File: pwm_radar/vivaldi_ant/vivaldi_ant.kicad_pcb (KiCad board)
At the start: 2 copper layers, 49.6 x 39.1 mm, 0 parts

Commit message: vivaldi antenna put in
vivaldi antenna put in
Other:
- board outline removed

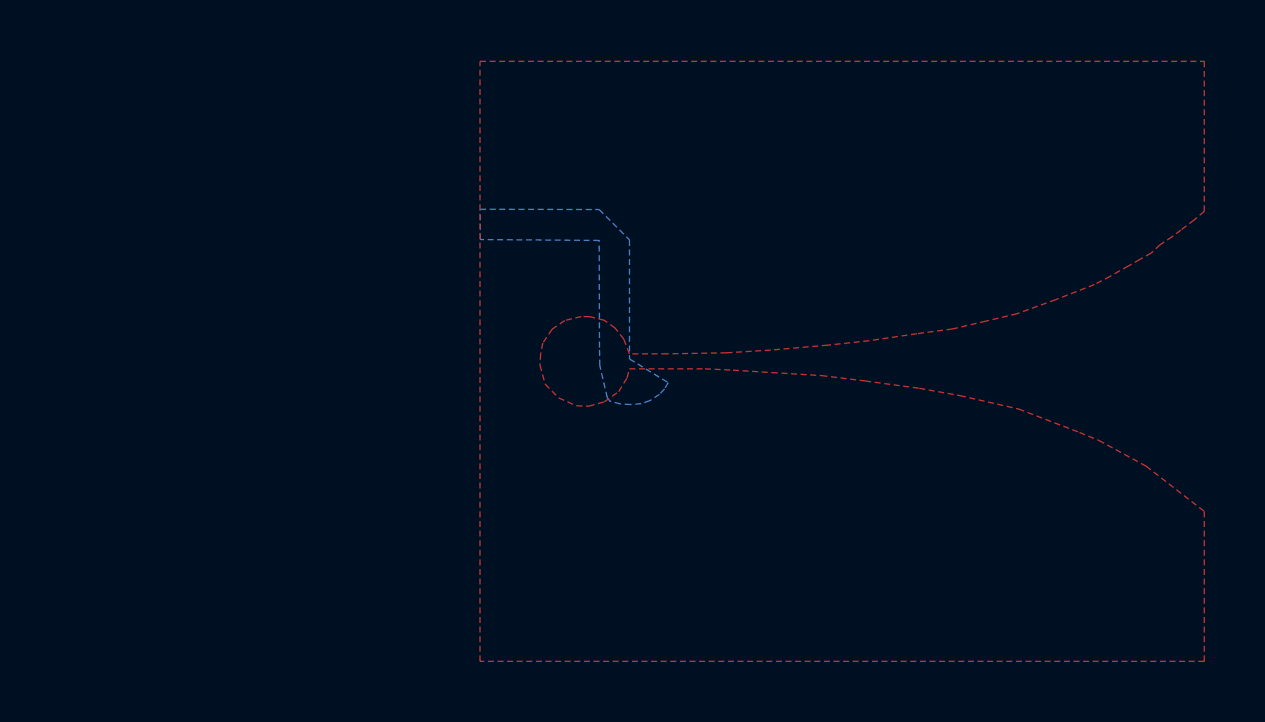
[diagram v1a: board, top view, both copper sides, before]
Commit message: added ant
added antenna
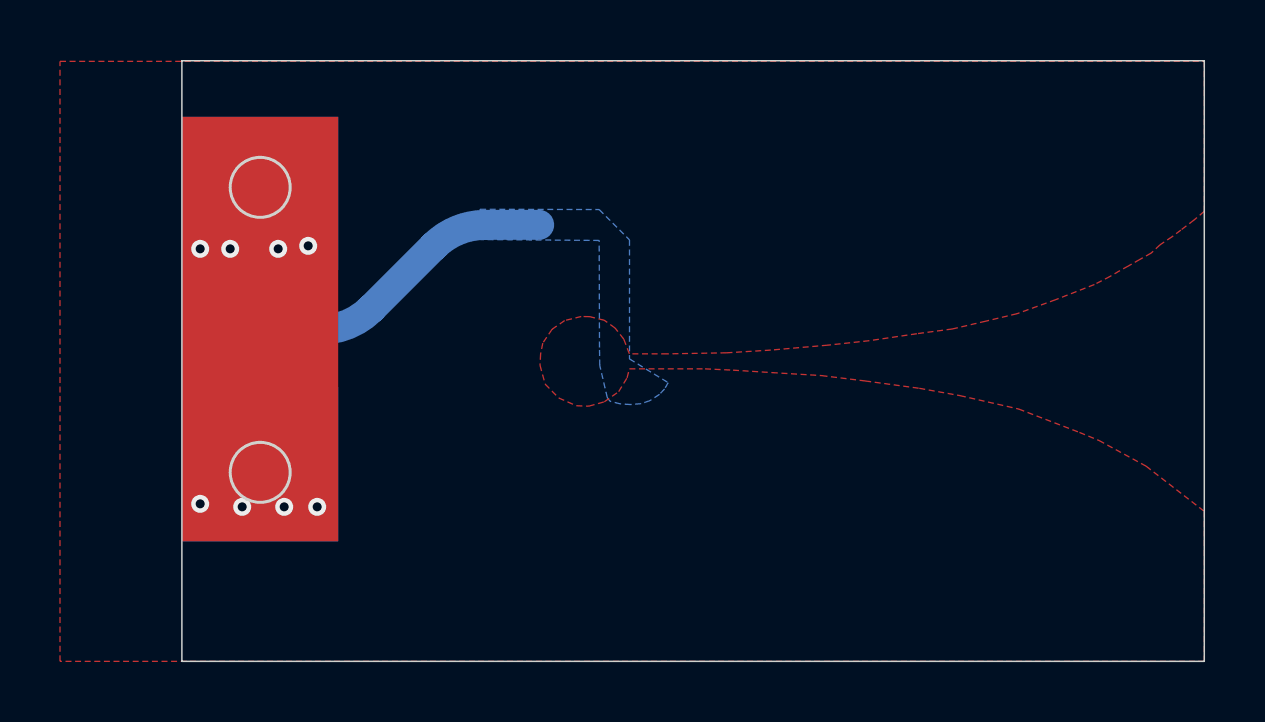
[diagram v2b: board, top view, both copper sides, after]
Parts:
- added J6: Conn_Coaxial, pwm_radar_lib:Wurth_RF_PWM_Conn, B.Cu at (144.5, 85.0)
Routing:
- net Net-(AE1-PCB_Trace): track 0.00 -> 12.6 mm
- net GND: vias 0 -> 8
- added copper zone on F.Cu, net GND
- added copper zone on B.Cu, net Net-(AE1-PCB_Trace)
- removed copper zone on B.Cu, net (none)
- removed copper zone on F.Cu, net (none)
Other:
- board outline added: 34.1 x 20 mm
